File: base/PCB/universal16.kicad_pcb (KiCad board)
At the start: 2 copper layers, 99.5 x 99.5 mm, 520 parts, among them J1 Conn_01x04, J10 Conn_01x01, J11 Conn_01x01, J12 Conn_01x01, J13 Conn_01x01, J14 Conn_01x03, J2 Conn_01x04, J3 Conn_01x03, J4 Conn_01x03, J5 Conn_01x04, J6 Conn_01x04, J7 Conn_01x03, J8 Conn_01x03, J9 Conn_01x03, SW1 SW_Push, SW10 SW_Push, SW11 SW_Push, SW12 SW_Push, SW13 SW_Push, SW14 SW_Push, SW15 SW_Push, SW16 SW_Push, SW2 SW_Push, SW3 SW_Push, SW4 SW_Push, SW5 SW_Push, SW6 SW_Push, SW7 SW_Push, SW8 SW_Push, SW9 SW_Push, U1 ProMicro

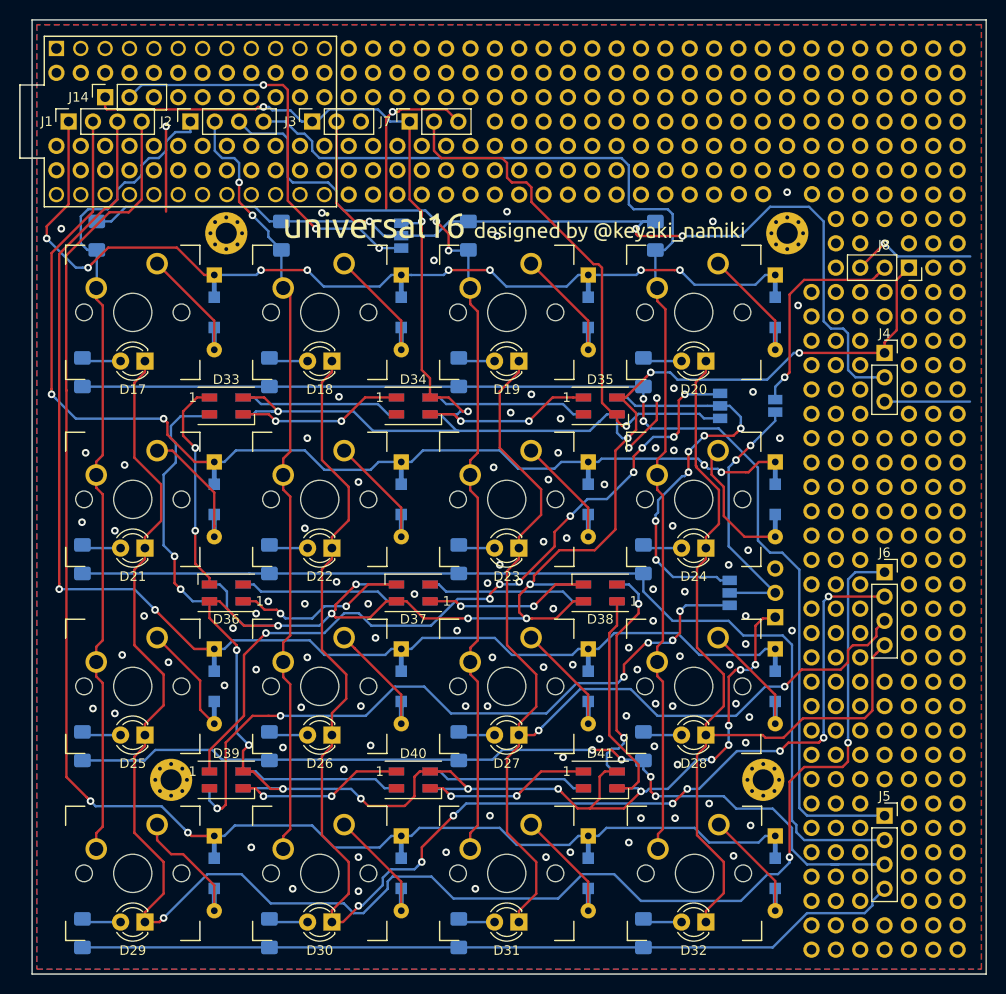
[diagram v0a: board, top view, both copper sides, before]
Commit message: update some footprints
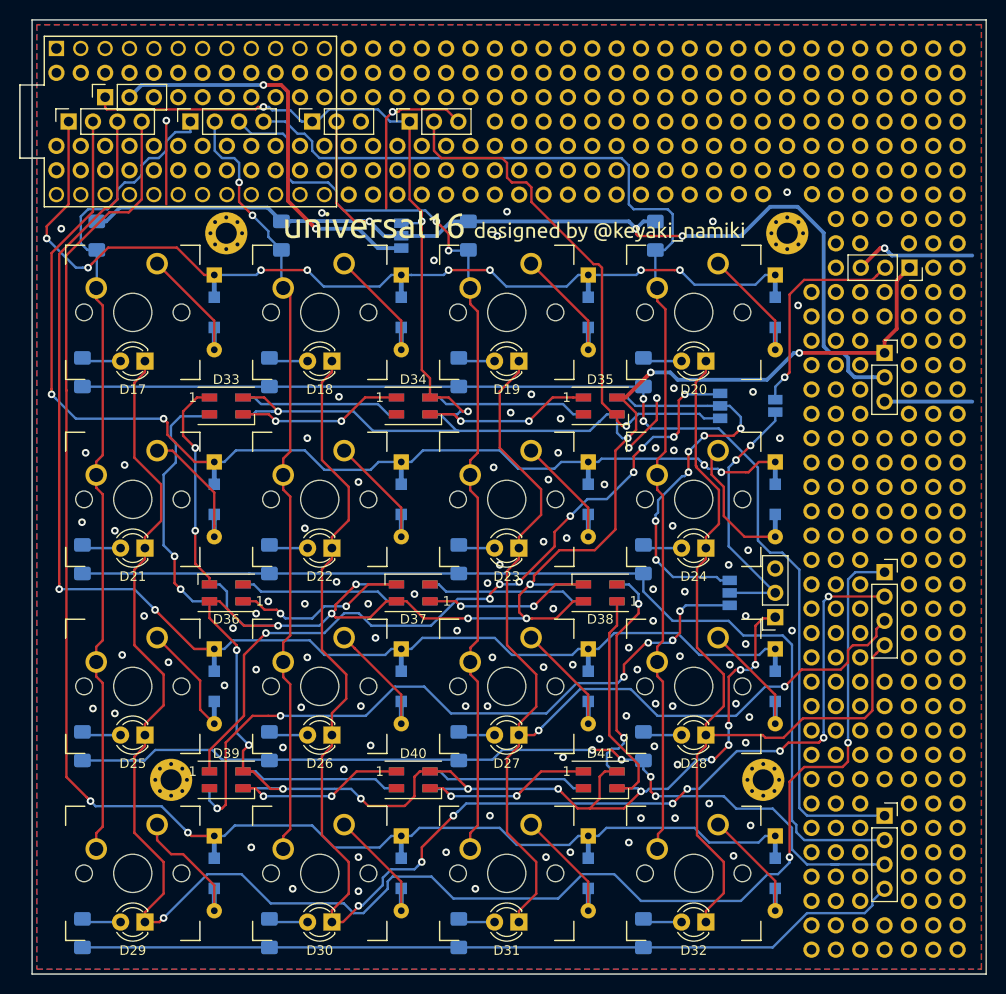
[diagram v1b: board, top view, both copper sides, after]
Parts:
- removed J1, J2, J5, J6: Conn_01x04, Connector_PinSocket_2.54mm:PinSocket_1x04_P2.54mm_Vertical
- removed J14, J3, J4, J7, J8: Conn_01x03, Connector_PinSocket_2.54mm:PinSocket_1x03_P2.54mm_Vertical
- added Col: Conn_01x04, myfootplint:PinSocket_1x04_P2.54mm_Vertical, B.Cu at (105.4, 71.1)
- added L-C: Conn_01x04, myfootplint:PinSocket_1x04_P2.54mm_Vertical, B.Cu at (177.8, 118.1)
- added L-R: Conn_01x04, myfootplint:PinSocket_1x04_P2.54mm_Vertical, B.Cu at (177.8, 143.5)
- added LED: Conn_01x03, myfootplint:PinSocket_1x03_P2.54mm_Vertical, B.Cu at (128.3, 71.1)
- added PWR: Conn_01x03, myfootplint:PinSocket_1x03_P2.54mm_Vertical, B.Cu at (96.5, 68.6)
- added ROW: Conn_01x04, myfootplint:PinSocket_1x04_P2.54mm_Vertical, B.Cu at (92.7, 71.1)
- added UG: Conn_01x03, myfootplint:PinSocket_1x03_P2.54mm_Vertical, B.Cu at (166.4, 122.8)
- added VCC: Conn_01x03, myfootplint:PinSocket_1x03_P2.54mm_Vertical, B.Cu at (118.1, 71.1)
- added VCC: Conn_01x03, myfootplint:PinSocket_1x03_P2.54mm_Vertical, B.Cu at (177.8, 95.2)
- J9: footprint Connector_PinSocket_2.54mm:PinSocket_1x03_P2.54mm_Vertical -> myfootplint:PinSocket_1x03_P2.54mm_Vertical
- moved J9 39.0 mm to (180.4, 86.4), turned to 90 degrees
- moved SW16 0.08 mm to (157.9, 149.5)
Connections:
- J9 pad 2: J9 -> Net-(J8-Pad2)
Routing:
- net VCC: track 119.3 -> 117.0 mm
- net +3V3: track 42.7 -> 42.6 mm, vias 3 -> 2
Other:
- net class wide added: clearance 0.2, trace_width 0.4, via_dia 0.8, via_drill 0.4
